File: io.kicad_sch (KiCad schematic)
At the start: 7 parts

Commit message: Separate IO from main board
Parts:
- D3: renamed from D?; footprint (none) -> LED_THT:LED_D4.0mm
- J2, J3: renamed from J?; footprint (none) -> Connector_PinHeader_2.54mm:PinHeader_1x02_P2.54mm_Vertical
- R32: renamed from R?; footprint (none) -> Resistor_SMD:R_0805_2012Metric
- gave numbers to parts that had none: 2

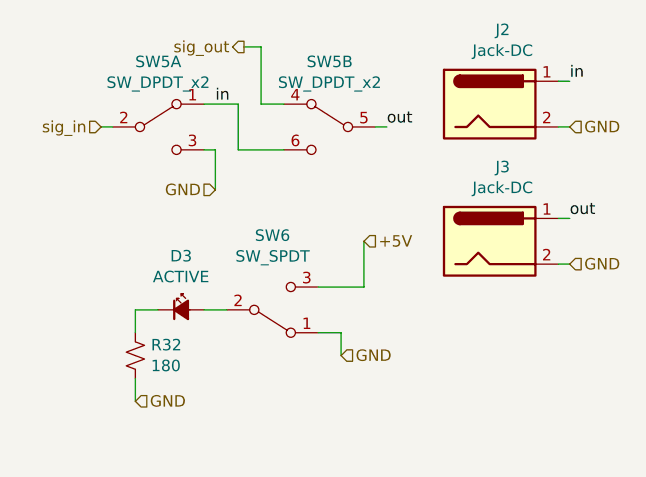
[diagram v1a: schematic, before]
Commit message: THT version
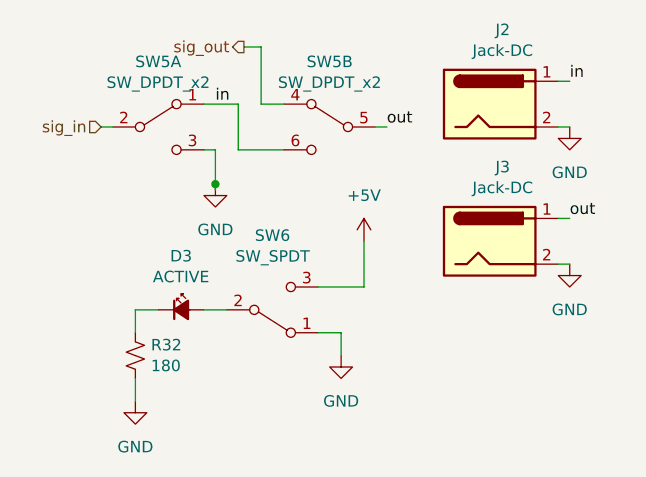
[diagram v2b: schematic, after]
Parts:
- R32: footprint Resistor_SMD:R_0805_2012Metric -> Resistor_THT:R_Axial_DIN0207_L6.3mm_D2.5mm_P7.62mm_Horizontal
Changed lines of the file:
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@@
 (kicad_sch (version 20230121) (generator eeschema)
   (paper "A4")
-  (wire (pts (xy 143.51 87.63) (xy 143.51 92.075))
+  (junction (at 143.51 91.44) (diameter 0) (color 0 0 0 0)
+  )
+  (wire (pts (xy 143.51 87.63) (xy 143.51 91.44))
     (stroke (width 0) (type default))
   )
   (wire (pts (xy 160.02 97.79) (xy 160.02 102.87))
+    (stroke (width 0) (type default))
+  )
+  (wire (pts (xy 143.51 91.44) (xy 143.51 92.075))
     (stroke (width 0) (type default))
   )
@@
     (effects (font (size 1.27 1.27)) (justify left bottom))
   )
-  (hierarchical_label "GND" (shape input) (at 182.88 100.33 0) (fields_autoplaced)
-    (effects (font (size 1.27 1.27)) (justify left))
-  )
-  (hierarchical_label "GND" (shape input) (at 157.48 110.49 0) (fields_autoplaced)
-    (effects (font (size 1.27 1.27)) (justify left))
-  )
-  (hierarchical_label "+5V" (shape input) (at 160.02 97.79 0) (fields_autoplaced)
-    (effects (font (size 1.27 1.27)) (justify left))
-  )
-  (hierarchical_label "GND" (shape input) (at 182.88 85.09 0) (fields_autoplaced)
-    (effects (font (size 1.27 1.27)) (justify left))
-  )
   (hierarchical_label "sig_out" (shape output) (at 146.685 76.2 180) (fields_autoplaced)
     (effects (font (size 1.27 1.27)) (justify right))
@@
     (effects (font (size 1.27 1.27)) (justify right))
   )
-  (hierarchical_label "GND" (shape input) (at 134.62 115.57 0) (fields_autoplaced)
-    (effects (font (size 1.27 1.27)) (justify left))
-  )
-  (hierarchical_label "GND" (shape input) (at 143.51 92.075 180) (fields_autoplaced)
-    (effects (font (size 1.27 1.27)) (justify right))
+  (symbol (lib_id "power:+5V") (at 160.02 97.79 0) (unit 1)
+    (in_bom yes) (on_board yes) (dnp no) (fields_autoplaced)
+    (property "Reference" "#PWR03" (at 160.02 101.6 0)
+      (effects (font (size 1.27 1.27)) hide)
+    )
+    (property "Value" "+5V" (at 160.02 92.71 0)
+      (effects (font (size 1.27 1.27)))
+    )
+    (property "Footprint" "" (at 160.02 97.79 0)
+      (effects (font (size 1.27 1.27)) hide)
+    )
+    (property "Datasheet" "" (at 160.02 97.79 0)
+      (effects (font (size 1.27 1.27)) hide)
+    )
+    (pin "1")
+    (instances
+      (project "tremolo"
+        (path "/0b4a96a2-bf10-4e32-96ec-f30d96cda1ff/eb2b1760-1b87-4424-b829-314a9e6ab15b"
+          (reference "#PWR03") (unit 1)
+        )
+      )
+    )
   )
   (symbol (lib_id "Device:R_Small_US") (at 134.62 110.49 0) (unit 1)
@@
       (effects (font (size 1.27 1.27)) (justify left))
     )
-    (property "Footprint" "Resistor_SMD:R_0805_2012Metric" (at 134.62 110.49 0)
+    (property "Footprint" "Resistor_THT:R_Axial_DIN0207_L6.3mm_D2.5mm_P7.62mm_Horizontal" (at 134.62 110.49 0)
       (effects (font (size 1.27 1.27)) hide)
     )
@@
     )
   )
+  (symbol (lib_id "power:GND") (at 182.88 85.09 0) (unit 1)
+    (in_bom yes) (on_board yes) (dnp no) (fields_autoplaced)
+    (property "Reference" "#PWR06" (at 182.88 91.44 0)
+      (effects (font (size 1.27 1.27)) hide)
+    )
+    (property "Value" "GND" (at 182.88 90.17 0)
+      (effects (font (size 1.27 1.27)))
+    )
+    (property "Footprint" "" (at 182.88 85.09 0)
+      (effects (font (size 1.27 1.27)) hide)
+    )
+    (property "Datasheet" "" (at 182.88 85.09 0)
+      (effects (font (size 1.27 1.27)) hide)
+    )
+    (pin "1")
+    (instances
+      (project "tremolo"
+        (path "/0b4a96a2-bf10-4e32-96ec-f30d96cda1ff/eb2b1760-1b87-4424-b829-314a9e6ab15b"
+          (reference "#PWR06") (unit 1)
+        )
+      )
+    )
+  )
   (symbol (lib_id "Connector:Jack-DC") (at 173.99 97.79 0) (unit 1)
     (in_bom yes) (on_board yes) (dnp no)
@@
     )
   )
+  (symbol (lib_id "power:GND") (at 134.62 115.57 0) (unit 1)
+    (in_bom yes) (on_board yes) (dnp no) (fields_autoplaced)
+    (property "Reference" "#PWR01" (at 134.62 121.92 0)
+      (effects (font (size 1.27 1.27)) hide)
+    )
+    (property "Value" "GND" (at 134.62 120.65 0)
+      (effects (font (size 1.27 1.27)))
+    )
+    (property "Footprint" "" (at 134.62 115.57 0)
+      (effects (font (size 1.27 1.27)) hide)
+    )
+    (property "Datasheet" "" (at 134.62 115.57 0)
+      (effects (font (size 1.27 1.27)) hide)
+    )
+    (pin "1")
+    (instances
+      (project "tremolo"
+        (path "/0b4a96a2-bf10-4e32-96ec-f30d96cda1ff/eb2b1760-1b87-4424-b829-314a9e6ab15b"
+          (reference "#PWR01") (unit 1)
+        )
+      )
+    )
+  )
   (symbol (lib_id "Connector:Jack-DC") (at 173.99 82.55 0) (unit 1)
     (in_bom yes) (on_board yes) (dnp no)
@@
         )
       )
+    )
+  )
+  (symbol (lib_id "power:GND") (at 143.51 91.44 0) (unit 1)
+    (in_bom yes) (on_board yes) (dnp no) (fields_autoplaced)
+    (property "Reference" "#PWR04" (at 143.51 97.79 0)
+      (effects (font (size 1.27 1.27)) hide)
+    )
+    (property "Value" "GND" (at 143.51 96.52 0)
+      (effects (font (size 1.27 1.27)))
+    )
+    (property "Footprint" "" (at 143.51 91.44 0)
+      (effects (font (size 1.27 1.27)) hide)
+    )
+    (property "Datasheet" "" (at 143.51 91.44 0)
+      (effects (font (size 1.27 1.27)) hide)
+    )
+    (pin "1")
+    (instances
+      (project "tremolo"
+        (path "/0b4a96a2-bf10-4e32-96ec-f30d96cda1ff/eb2b1760-1b87-4424-b829-314a9e6ab15b"
+          (reference "#PWR04") (unit 1)
+        )
+      )
+    )
+  )
+  (symbol (lib_id "power:GND") (at 157.48 110.49 0) (unit 1)
+    (in_bom yes) (on_board yes) (dnp no) (fields_autoplaced)
+    (property "Reference" "#PWR02" (at 157.48 116.84 0)
+      (effects (font (size 1.27 1.27)) hide)
+    )
+    (property "Value" "GND" (at 157.48 115.57 0)
+      (effects (font (size 1.27 1.27)))
+    )
+    (property "Footprint" "" (at 157.48 110.49 0)
+      (effects (font (size 1.27 1.27)) hide)
+    )
+    (property "Datasheet" "" (at 157.48 110.49 0)
+      (effects (font (size 1.27 1.27)) hide)
+    )
+    (pin "1")
+    (instances
+      (project "tremolo"
+        (path "/0b4a96a2-bf10-4e32-96ec-f30d96cda1ff/eb2b1760-1b87-4424-b829-314a9e6ab15b"
+          (reference "#PWR02") (unit 1)
+        )
+      )
+    )
+  )
+  (symbol (lib_id "power:GND") (at 182.88 100.33 0) (unit 1)
+    (in_bom yes) (on_board yes) (dnp no) (fields_autoplaced)
+    (property "Reference" "#PWR05" (at 182.88 106.68 0)
+      (effects (font (size 1.27 1.27)) hide)
+    )
+    (property "Value" "GND" (at 182.88 105.41 0)
+      (effects (font (size 1.27 1.27)))
+    )
+    (property "Footprint" "" (at 182.88 100.33 0)
+      (effects (font (size 1.27 1.27)) hide)
+    )
+    (property "Datasheet" "" (at 182.88 100.33 0)
+      (effects (font (size 1.27 1.27)) hide)
+    )
+    (pin "1")
+    (instances
+      (project "tremolo"
+        (path "/0b4a96a2-bf10-4e32-96ec-f30d96cda1ff/eb2b1760-1b87-4424-b829-314a9e6ab15b"
+          (reference "#PWR05") (unit 1)
+        )
+      )
